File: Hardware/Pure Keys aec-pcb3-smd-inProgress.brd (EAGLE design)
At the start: 158.7 x 51.7 mm, 72 parts, among them Q2 20MHz, U1 ATMEGA328P_TQFP

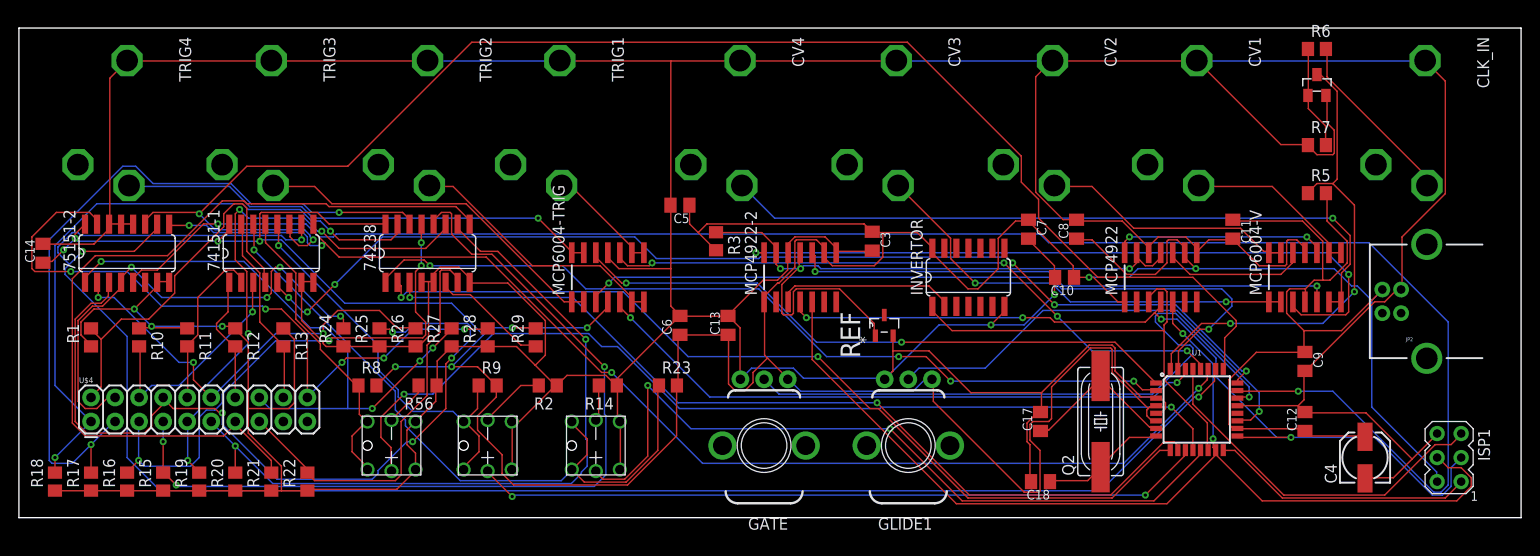
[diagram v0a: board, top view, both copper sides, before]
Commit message: Replaced Sockets with vertical type
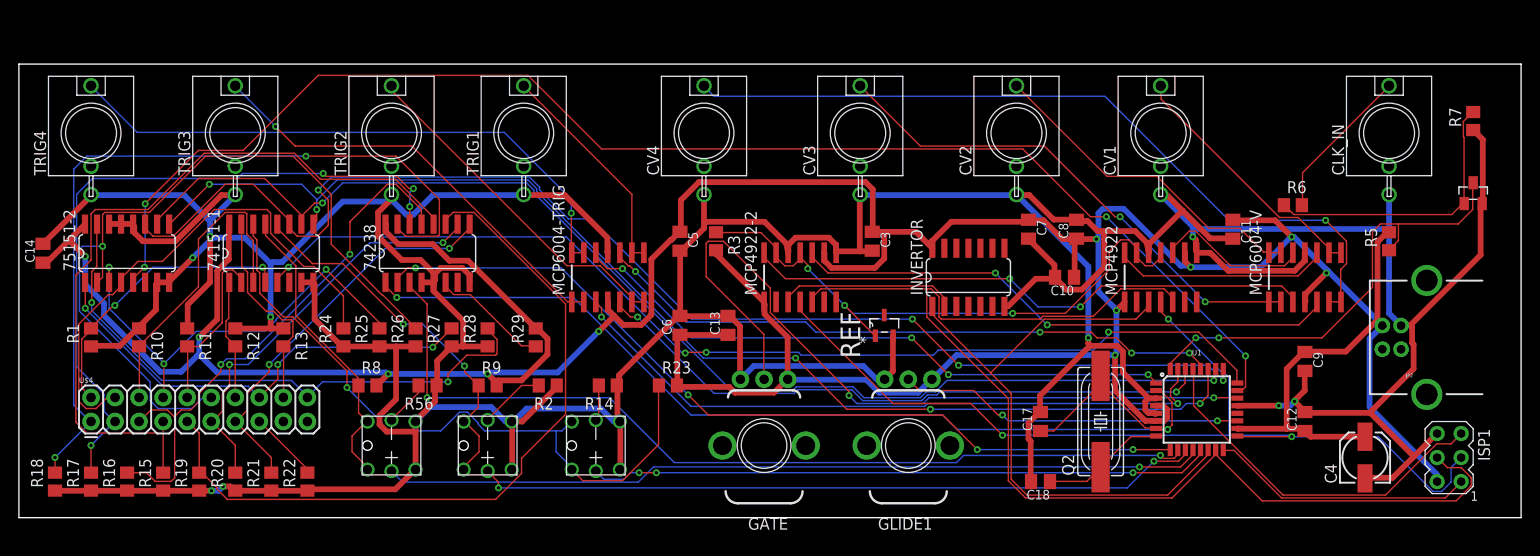
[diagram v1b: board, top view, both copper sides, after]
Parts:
- CLK_IN, CV1, CV2, CV3, CV4, TRIG1, TRIG2, TRIG3, TRIG4: value PJ302M -> S_JACK; device GMSN:PJ302M -> INSTRUO:S_JACK
- moved CLOCK 20.1 mm to (153.7, 27.9)
- moved R6 16.7 mm to (134.6, 26.7)
- moved R7 16.7 mm to (153.7, 35.6), turned to 90 degrees
- moved CLK_IN 10.9 mm to (144.8, 34.3), turned to 0 degrees
- moved CV2 10.9 mm to (105.4, 34.3), turned to 0 degrees
- moved CV4 10.9 mm to (72.4, 34.3), turned to 0 degrees
- moved TRIG1 10.9 mm to (53.3, 34.3), turned to 0 degrees
- moved TRIG2 10.9 mm to (39.4, 34.3), turned to 0 degrees
- moved TRIG3 10.9 mm to (22.9, 34.3), turned to 0 degrees
- moved TRIG4 10.9 mm to (7.62, 34.3), turned to 0 degrees
- moved CV1 10.9 mm to (120.7, 34.3), turned to 0 degrees
- moved CV3 10.9 mm to (88.9, 34.3), turned to 0 degrees
- moved R5 9.16 mm to (144.8, 22.9), turned to 90 degrees
- moved C5 3.81 mm to (69.8, 22.9), turned to 270 degrees
- moved JP2 3.81 mm to (146.1, 12.7)
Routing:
- net GND: track 709.3 -> 632.3 mm, vias 5 -> 9
- net A1IN: track 187.8 -> 130.8 mm, vias 3 -> 2
- net 5V: track 483.5 -> 434.7 mm, vias 10 -> 11
- net T6: track 87.5 -> 42.1 mm, vias 0 -> 2
- net DBIN: track 190.6 -> 147.3 mm, vias 2 -> 4
- net BR1: track 87.0 -> 47.7 mm, vias 4 -> 3
- net BR2: track 45.8 -> 82.7 mm, vias 3 -> 1
- net T7: track 44.0 -> 7.53 mm
- net T5: track 78.5 -> 43.8 mm
- net A0IN: track 162.0 -> 136.3 mm, vias 2 -> 4
- net T4: track 56.6 -> 79.7 mm, vias 4 -> 0
- net N$17: track 11.0 -> 30.1 mm
- net CS1: track 47.6 -> 65.5 mm
- net MOSI: track 110.8 -> 128.1 mm, vias 2 -> 0
- net T0: track 68.0 -> 84.5 mm
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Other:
- board size 158.7 x 51.7 mm -> 158.7 x 47.9 mm
